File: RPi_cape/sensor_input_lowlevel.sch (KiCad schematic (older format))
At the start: 37 parts, among them U17 LM2903, U4 AD8552A

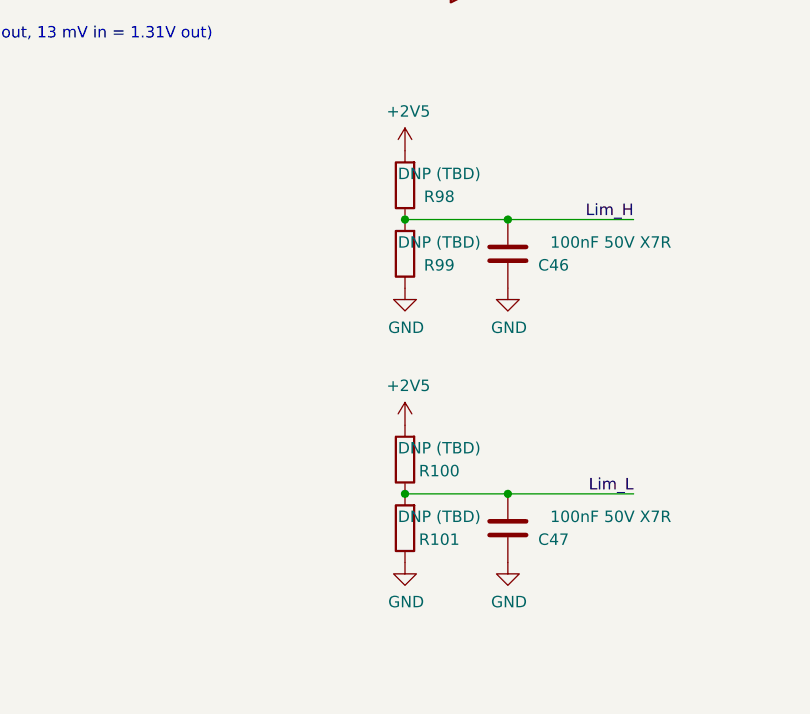
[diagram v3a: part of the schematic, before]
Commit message: Manufacturing clean-up
Corrections and additions to BOM etc. for manufacturing
Added power draw tracking spreadsheet
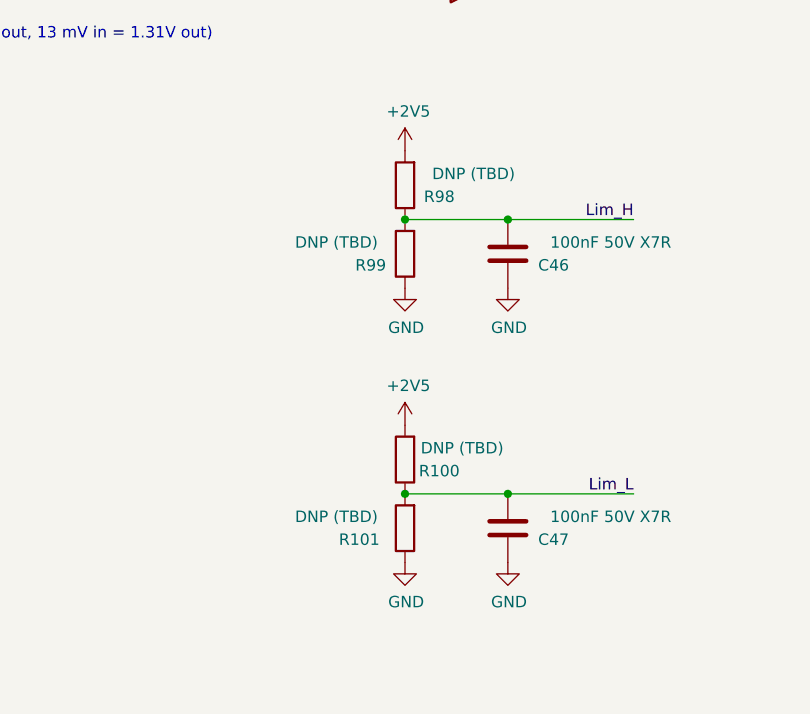
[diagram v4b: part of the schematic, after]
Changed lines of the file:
@@
 AR Path="/5E8AA959/5EDD8202" Ref="R98"  Part="1"
 F 0 "R98" H 8050 4050 50  0000 C CNN
-F 1 "DNP (TBD)" H 8050 3950 50  0000 C CNN
+F 1 "DNP (TBD)" H 7900 3950 50  0000 C CNN
 F 2 "Resistor_SMD:R_1206_3216Metric" V 8130 4000 50  0001 C CNN
 F 3 "~" H 8200 4000 50  0001 C CNN
@@
 AR Path="/5E8A4ABF/5EDD8208" Ref="R?"  Part="1"
 AR Path="/5E8AA959/5EDD8208" Ref="R99"  Part="1"
-F 0 "R99" H 8050 4350 50  0000 C CNN
-F 1 "DNP (TBD)" H 8050 4250 50  0000 C CNN
+F 0 "R99" H 8350 4350 50  0000 C CNN
+F 1 "DNP (TBD)" H 8500 4250 50  0000 C CNN
 F 2 "Resistor_SMD:R_1206_3216Metric" V 8130 4300 50  0001 C CNN
 F 3 "~" H 8200 4300 50  0001 C CNN
@@
 AR Path="/5E8AA959/5EDD822B" Ref="R100"  Part="1"
 F 0 "R100" H 8050 5250 50  0000 C CNN
-F 1 "DNP (TBD)" H 8050 5150 50  0000 C CNN
+F 1 "DNP (TBD)" H 7950 5150 50  0000 C CNN
 F 2 "Resistor_SMD:R_1206_3216Metric" V 8130 5200 50  0001 C CNN
 F 3 "~" H 8200 5200 50  0001 C CNN
@@
 AR Path="/5E8A4ABF/5EDD8231" Ref="R?"  Part="1"
 AR Path="/5E8AA959/5EDD8231" Ref="R101"  Part="1"
-F 0 "R101" H 8050 5550 50  0000 C CNN
-F 1 "DNP (TBD)" H 8050 5450 50  0000 C CNN
+F 0 "R101" H 8400 5550 50  0000 C CNN
+F 1 "DNP (TBD)" H 8500 5450 50  0000 C CNN
 F 2 "Resistor_SMD:R_1206_3216Metric" V 8130 5500 50  0001 C CNN
 F 3 "~" H 8200 5500 50  0001 C CNN
